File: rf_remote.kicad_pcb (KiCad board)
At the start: 2 copper layers, 57.3 x 26.5 mm, 25 parts, among them J1 10118194-0001LF, P1 CONN_01X04, P2 CONN_01X01, U1 SAMD21E18, U2 RFM69CW-915MHZ, U3 MIC5504-3.3YM5-T5

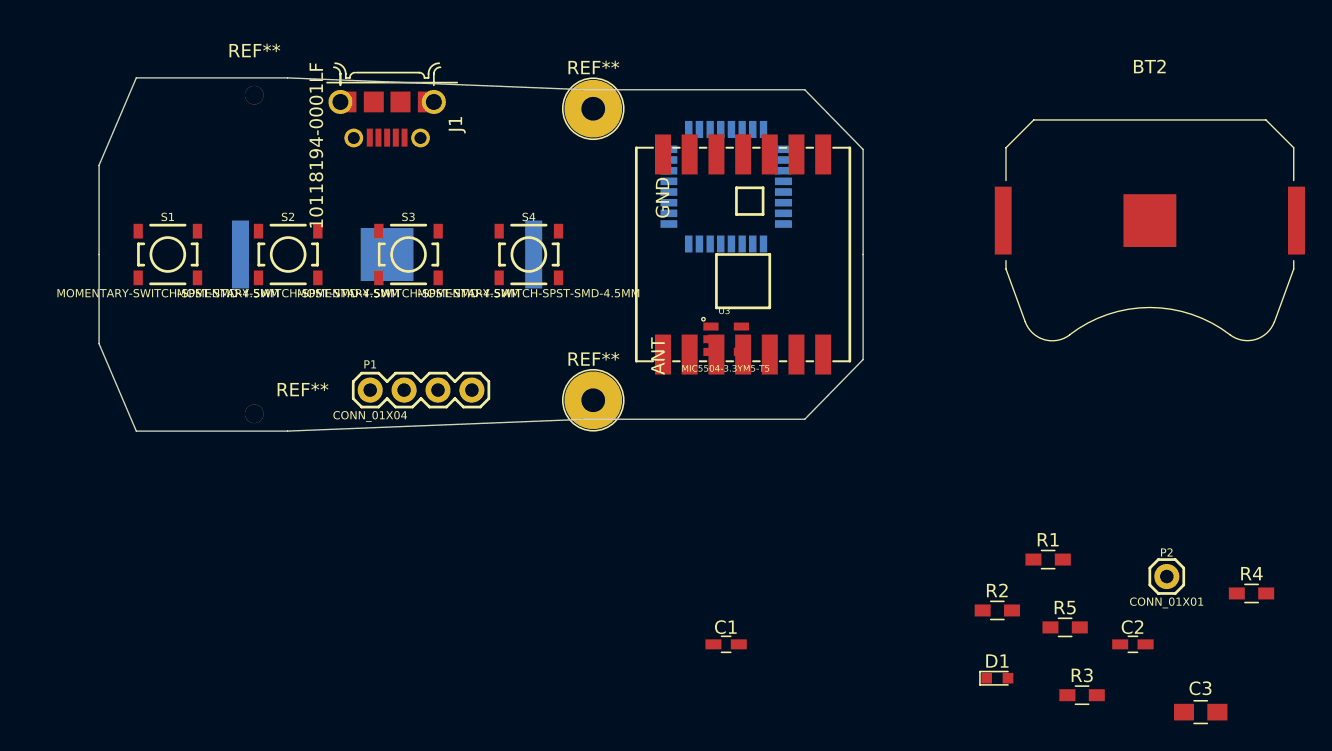
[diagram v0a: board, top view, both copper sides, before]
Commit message: Removed second battery, updated PCB layout
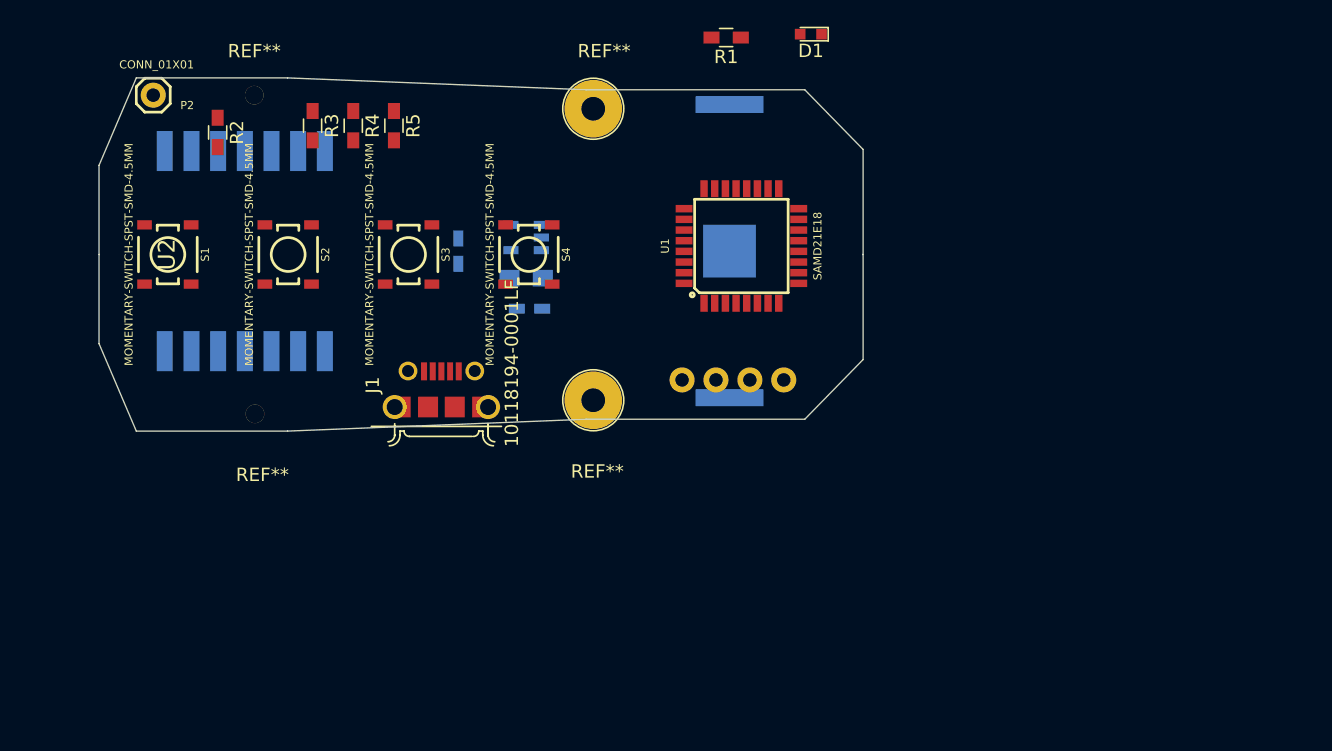
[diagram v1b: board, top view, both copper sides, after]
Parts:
- removed BT2: 3.3V battery, Battery_Holders:Keystone_3034_1x20mm-CoinCell
- BT1: value 3.3V battery -> 6V battery
- C1, C2, C3, P1, U2, U3: moved to B.Cu
- U1: moved to F.Cu
- moved P2 84.1 mm to (80.3, 64.3)
- moved R4 75.9 mm to (95.2, 66.5), turned to 270 degrees
- moved R3 71.7 mm to (92.2, 66.5), turned to 270 degrees
- moved R2 68.5 mm to (85.1, 67.1), turned to 270 degrees
- moved R5 62.8 mm to (98.3, 66.5), turned to 270 degrees
- moved C3 60.1 mm to (108.2, 78.0), turned to 180 degrees
- moved C2 51.7 mm to (108.5, 80.3), turned to 180 degrees
- moved D1 50.2 mm to (129.5, 59.7), turned to 180 degrees
- moved R1 46.0 mm to (123.2, 59.9), turned to 180 degrees
- moved U2 37.3 mm to (87.1, 75.9), turned to 270 degrees
- moved C1 35.6 mm to (103.1, 75.9), turned to 270 degrees
- moved BT1 25.7 mm to (123.4, 75.9), turned to 270 degrees
- moved P1 23.4 mm to (119.9, 85.6)
- moved J1 23.2 mm to (101.9, 87.6), turned to 0 degrees
- moved U3 16.8 mm to (108.2, 74.9), turned to 180 degrees
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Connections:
- BT1 pad 1: +3V3 -> +6V
- C2 pad 1: +5V -> +6V
- C3 pad 1: +5V -> +6V
- U1 pad 1: SW1 -> SW4
- U1 pad 11: RADIO_MOSI -> Net-(U1-Pad11)
- U1 pad 12: RADIO_SCK -> Net-(U1-Pad12)
- U1 pad 13: RADIO_MISO -> Net-(U1-Pad13)
- U1 pad 14: RADIO_NSS -> Net-(U1-Pad14)
- U1 pad 17: Net-(U1-Pad17) -> RADIO_MOSI
- U1 pad 18: Net-(U1-Pad18) -> RADIO_SCK
- U1 pad 19: Net-(U1-Pad19) -> RADIO_MISO
- U1 pad 2: SW2 -> Net-(U1-Pad2)
- U1 pad 20: Net-(U1-Pad20) -> RADIO_NSS
- U1 pad 4: SW4 -> Net-(U1-Pad4)
- U1 pad 5: Net-(U1-Pad5) -> SW2
- U1 pad 7: Net-(U1-Pad7) -> SW1
- U3 pad 1: +5V -> +6V
- U3 pad 3: +5V -> +6V

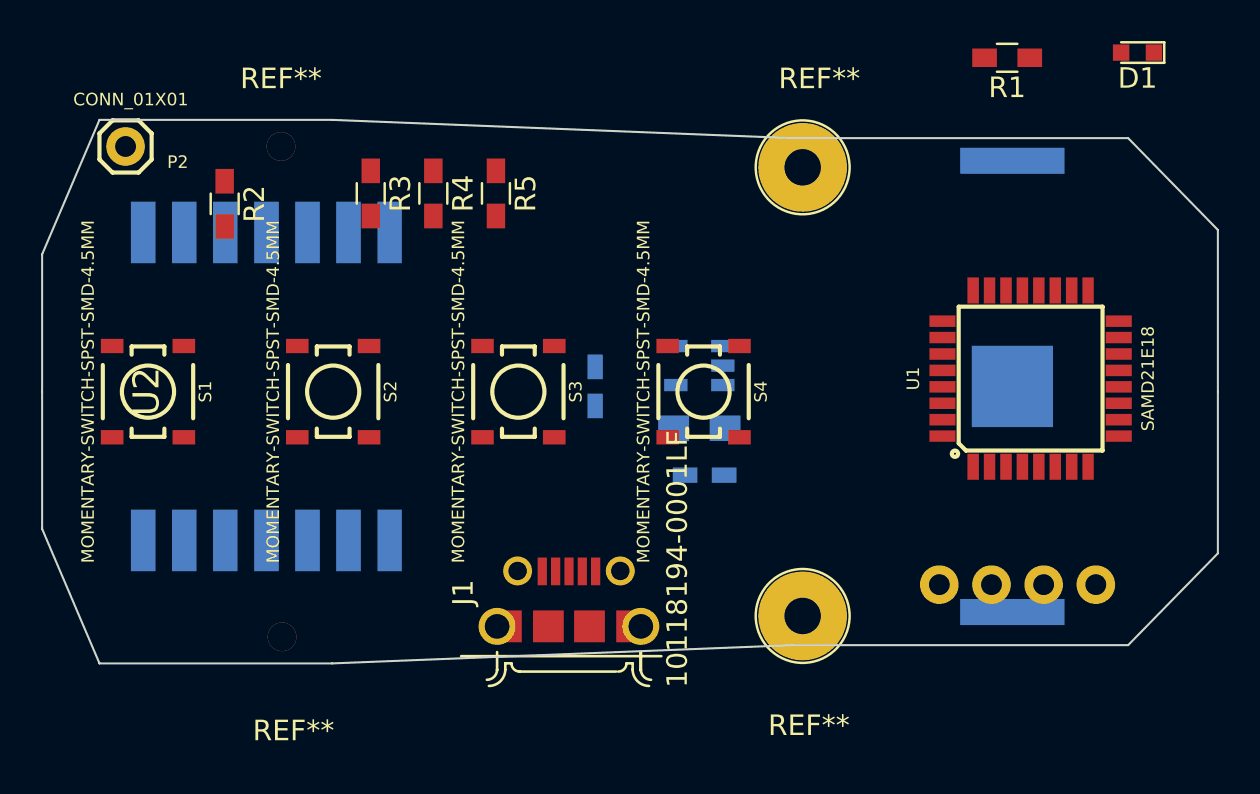
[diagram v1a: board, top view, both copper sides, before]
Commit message: Removed linear reg & USB port. Draft of layout and routing.
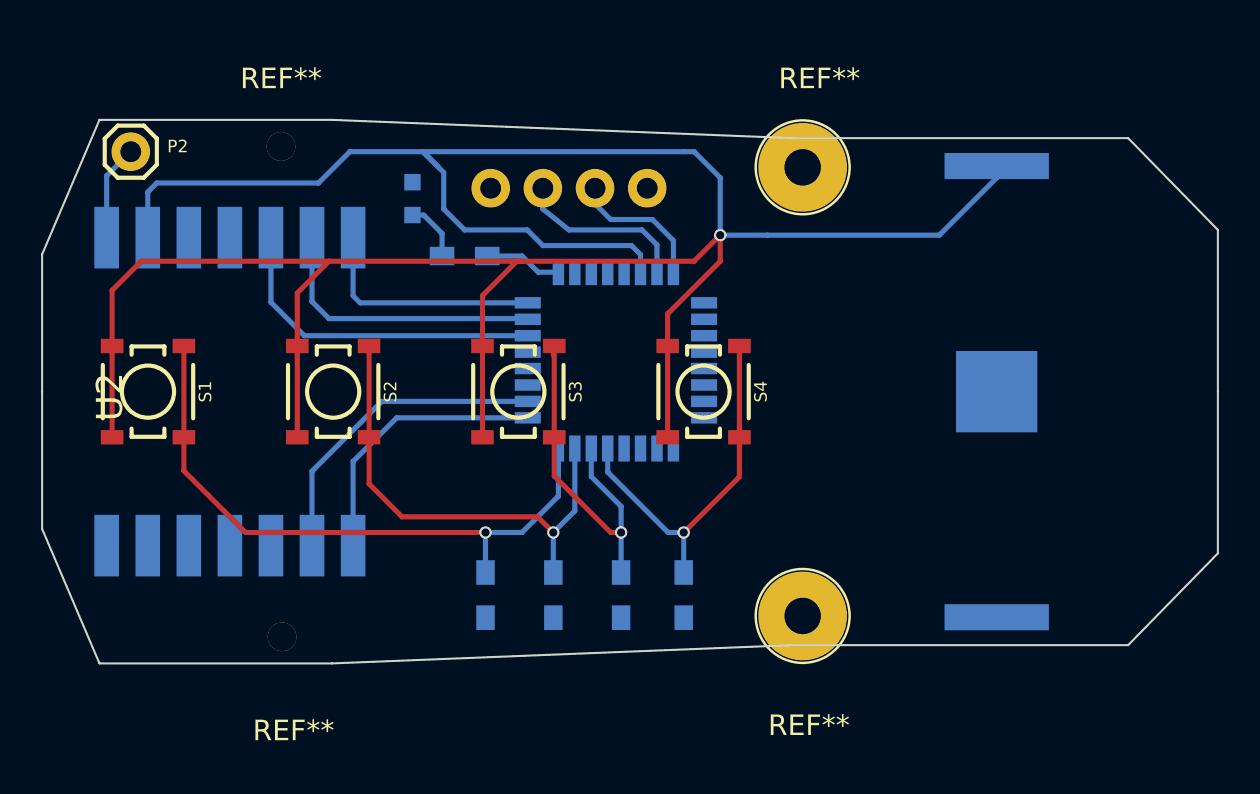
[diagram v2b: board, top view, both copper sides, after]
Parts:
- removed C1, C2: 1uF, Capacitors_SMD:C_0603_HandSoldering
- removed C3: 10uF, Capacitors_SMD:C_0805_HandSoldering
- removed J1: 10118194-0001LF, 10118194-0001LF:FRAMATOME_10118194-0001LF
- removed U3: MIC5504-3.3YM5-T5, MIC5504-3.3YM5-T5:SOT23-5P95_280X145XL45X37N
- BT1: value 6V battery -> 3V battery
- D1, R1, R2, R3, R4, R5, U1: moved to B.Cu
- moved D1 36.0 mm to (94.2, 66.8), turned to 270 degrees
- moved R1 28.1 mm to (96.8, 69.6), turned to 0 degrees
- moved P1 24.0 mm to (105.7, 66.3), turned to 180 degrees
- moved R2 22.9 mm to (97.8, 86.1), turned to 90 degrees
- moved R4 21.6 mm to (104.4, 86.1), turned to 90 degrees
- moved R5 21.6 mm to (107.4, 86.1), turned to 90 degrees
- moved R3 21.5 mm to (101.1, 86.1), turned to 90 degrees
- moved U1 20.2 mm to (104.1, 74.7), turned to 180 degrees
- moved U2 1.80 mm to (85.3, 76.2)
- moved BT1 0.80 mm to (122.7, 76.2)
- moved P2 0.36 mm to (80.5, 64.5)
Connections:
- BT1 pad 1: +6V -> +3V3
- P1 pad 1: Net-(P1-Pad1) -> +3V3
- P1 pad 2: Net-(P1-Pad2) -> ARM_SWDIO
- P1 pad 3: Net-(P1-Pad3) -> ARM_SWCLK
- P1 pad 4: Net-(P1-Pad4) -> GND
- U1 pad 1: SW4 -> Net-(U1-Pad1)
- U1 pad 13: Net-(U1-Pad13) -> SW4
- U1 pad 14: Net-(U1-Pad14) -> SW3
- U1 pad 15: Net-(U1-Pad15) -> SW2
- U1 pad 16: Net-(U1-Pad16) -> SW1
- U1 pad 17: RADIO_MOSI -> RADIO_MISO
- U1 pad 18: RADIO_SCK -> RADIO_DIO0
- U1 pad 19: RADIO_MISO -> Net-(U1-Pad19)
- U1 pad 20: RADIO_NSS -> Net-(U1-Pad20)
- U1 pad 22: Net-(U1-Pad22) -> RADIO_MOSI
- U1 pad 23: USB_D- -> RADIO_SCK
- U1 pad 24: USB_D+ -> RADIO_NSS
- U1 pad 27: RADIO_DIO0 -> Net-(U1-Pad27)
- U1 pad 3: SW3 -> Net-(U1-Pad3)
- U1 pad 5: SW2 -> Net-(U1-Pad5)
- U1 pad 7: SW1 -> Net-(U1-Pad7)
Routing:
- net +3V3: track 0.00 -> 132.6 mm, vias 0 -> 1
- net SW1: track 0.06 -> 30.6 mm, vias 0 -> 1
- net SW2: track 0.11 -> 23.3 mm, vias 0 -> 1
- net SW4: track 0.00 -> 18.2 mm, vias 0 -> 1
- net SW3: track 0.06 -> 17.9 mm, vias 0 -> 1
- net RADIO_MOSI: track 0.00 -> 16.3 mm
- net RADIO_DIO0: track 0.00 -> 15.5 mm
- net RADIO_SCK: track 0.00 -> 14.0 mm
- net RADIO_MISO: track 0.00 -> 13.5 mm
- net RADIO_NSS: track 0.00 -> 11.5 mm
- net ARM_SWCLK: track 0.00 -> 9.07 mm
- net ARM_SWDIO: track 0.00 -> 7.37 mm
- net ANTENNA: track 0.00 -> 4.67 mm
- net SIMPLE_LED: track 0.00 -> 3.79 mm
- net Net-(D1-Pad2): track 0.00 -> 2.91 mm

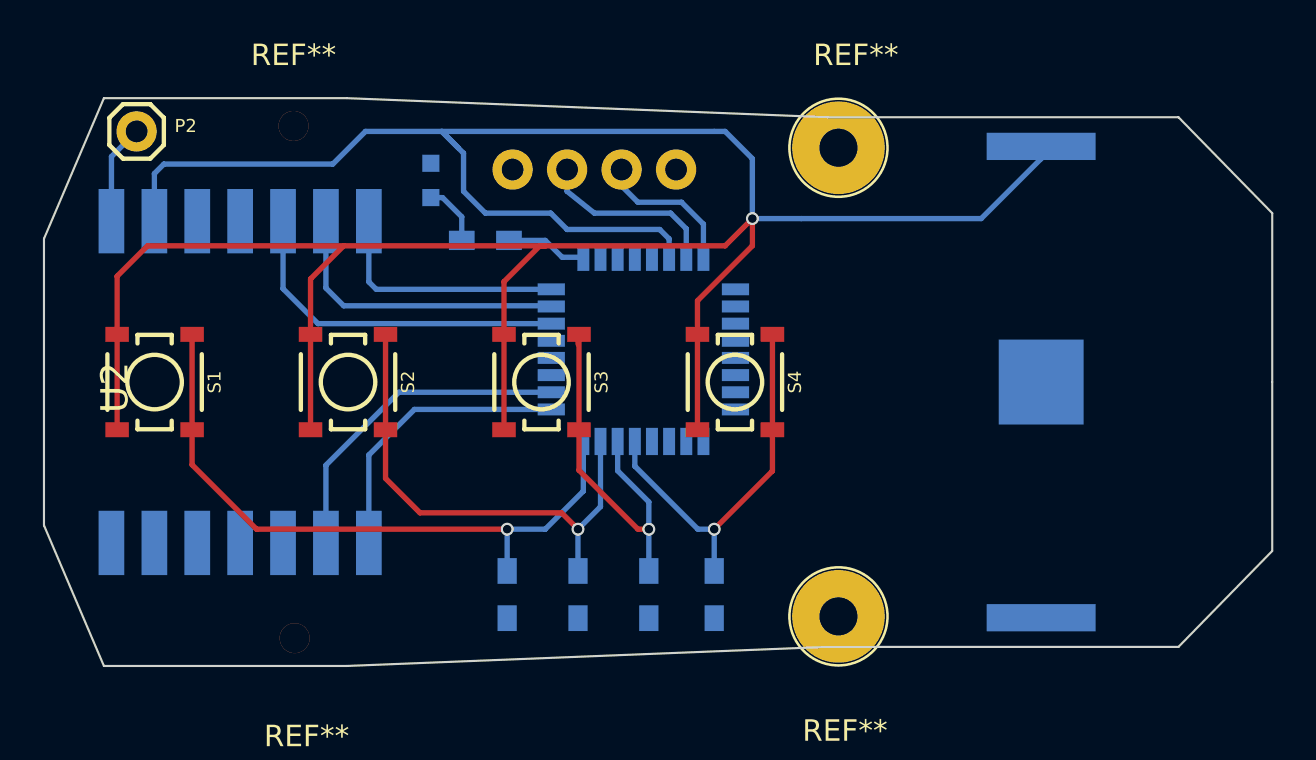
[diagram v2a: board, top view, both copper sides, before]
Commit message: removed pulldowns
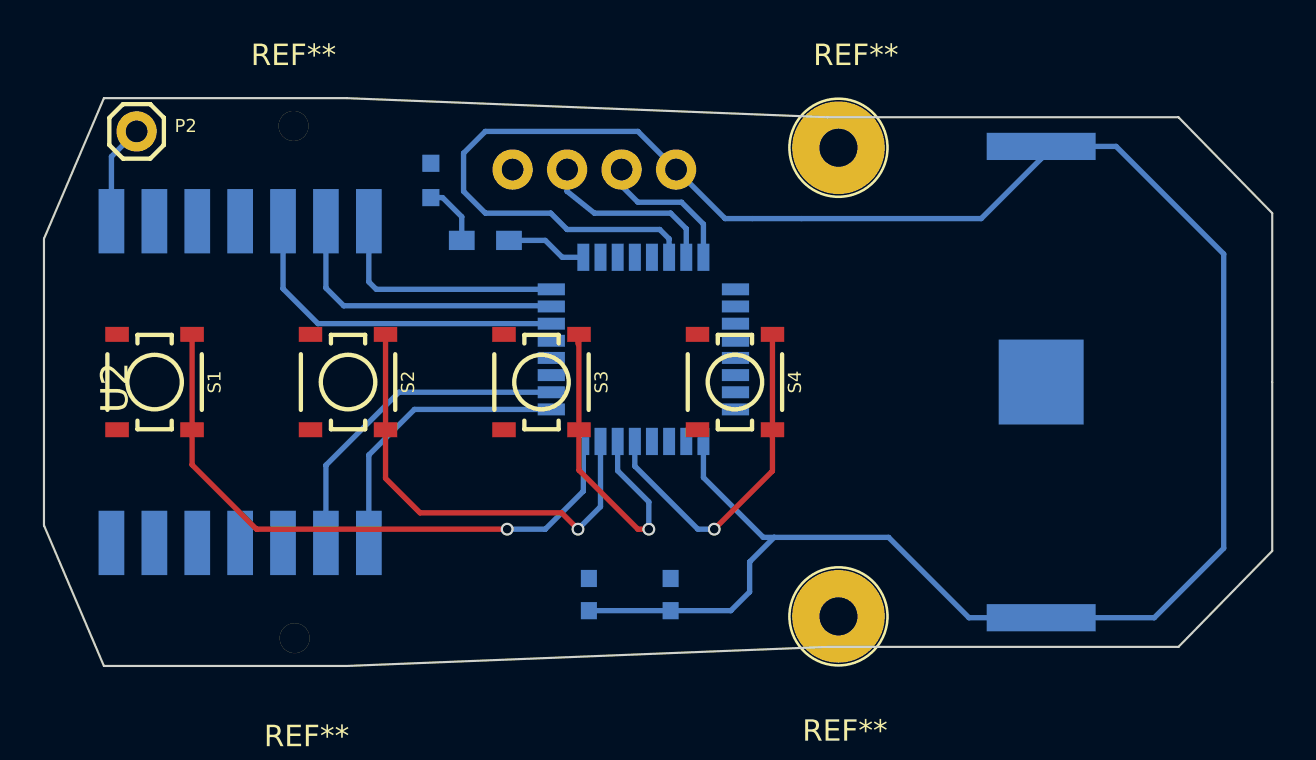
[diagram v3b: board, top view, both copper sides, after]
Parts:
- removed R2, R3, R4, R5: 10K, Resistors_SMD:R_0603_HandSoldering
- added C1: 1.0UF-0603-16V-10%, Capacitors_SMD:C_0603, B.Cu at (105.4, 86.1)
- added C2: 10UF-0603-6.3V-20%, Capacitors_SMD:C_0603, B.Cu at (101.6, 86.1)
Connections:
- S1 pad 2: +3V3 -> GND
- S1 pad 3: +3V3 -> GND
- S2 pad 2: +3V3 -> GND
- S2 pad 3: +3V3 -> GND
- S3 pad 2: +3V3 -> GND
- S3 pad 3: +3V3 -> GND
- S4 pad 2: +3V3 -> GND
- S4 pad 3: +3V3 -> GND
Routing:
- net +3V3: track 132.6 -> 109.0 mm, vias 1 -> 0
- net SW4: track 18.2 -> 16.3 mm
- net SW2: track 23.3 -> 21.3 mm
- net SW1: track 30.6 -> 28.7 mm
- net SW3: track 17.9 -> 15.9 mm
